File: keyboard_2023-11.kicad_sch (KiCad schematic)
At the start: 74 parts, among them J1 Conn_01x04, J11 Conn_01x07_Socket, J2 Conn_01x04_Socket, J3 Conn_01x07_Socket, J4 Conn_01x07_Pin, SW1 SW_Push, SW10 SW_Push, SW11 SW_Push, SW12 SW_Push, SW13 SW_Push, SW14 SW_Push, SW15 SW_Push, SW16 SW_Push, SW17 SW_Push, SW18 SW_Push, SW19 SW_Push, SW2 SW_Push, SW20 SW_Push, SW21 SW_Push, SW22 SW_Push, SW23 SW_Push, SW24 SW_Push, SW3 SW_Push, SW4 SW_Push, SW5 SW_Push, SW6 SW_Push, SW7 SW_Push, SW8 SW_Push, SW9 SW_Push, U1 MCP23017_SO, U2 MCP23017_SO

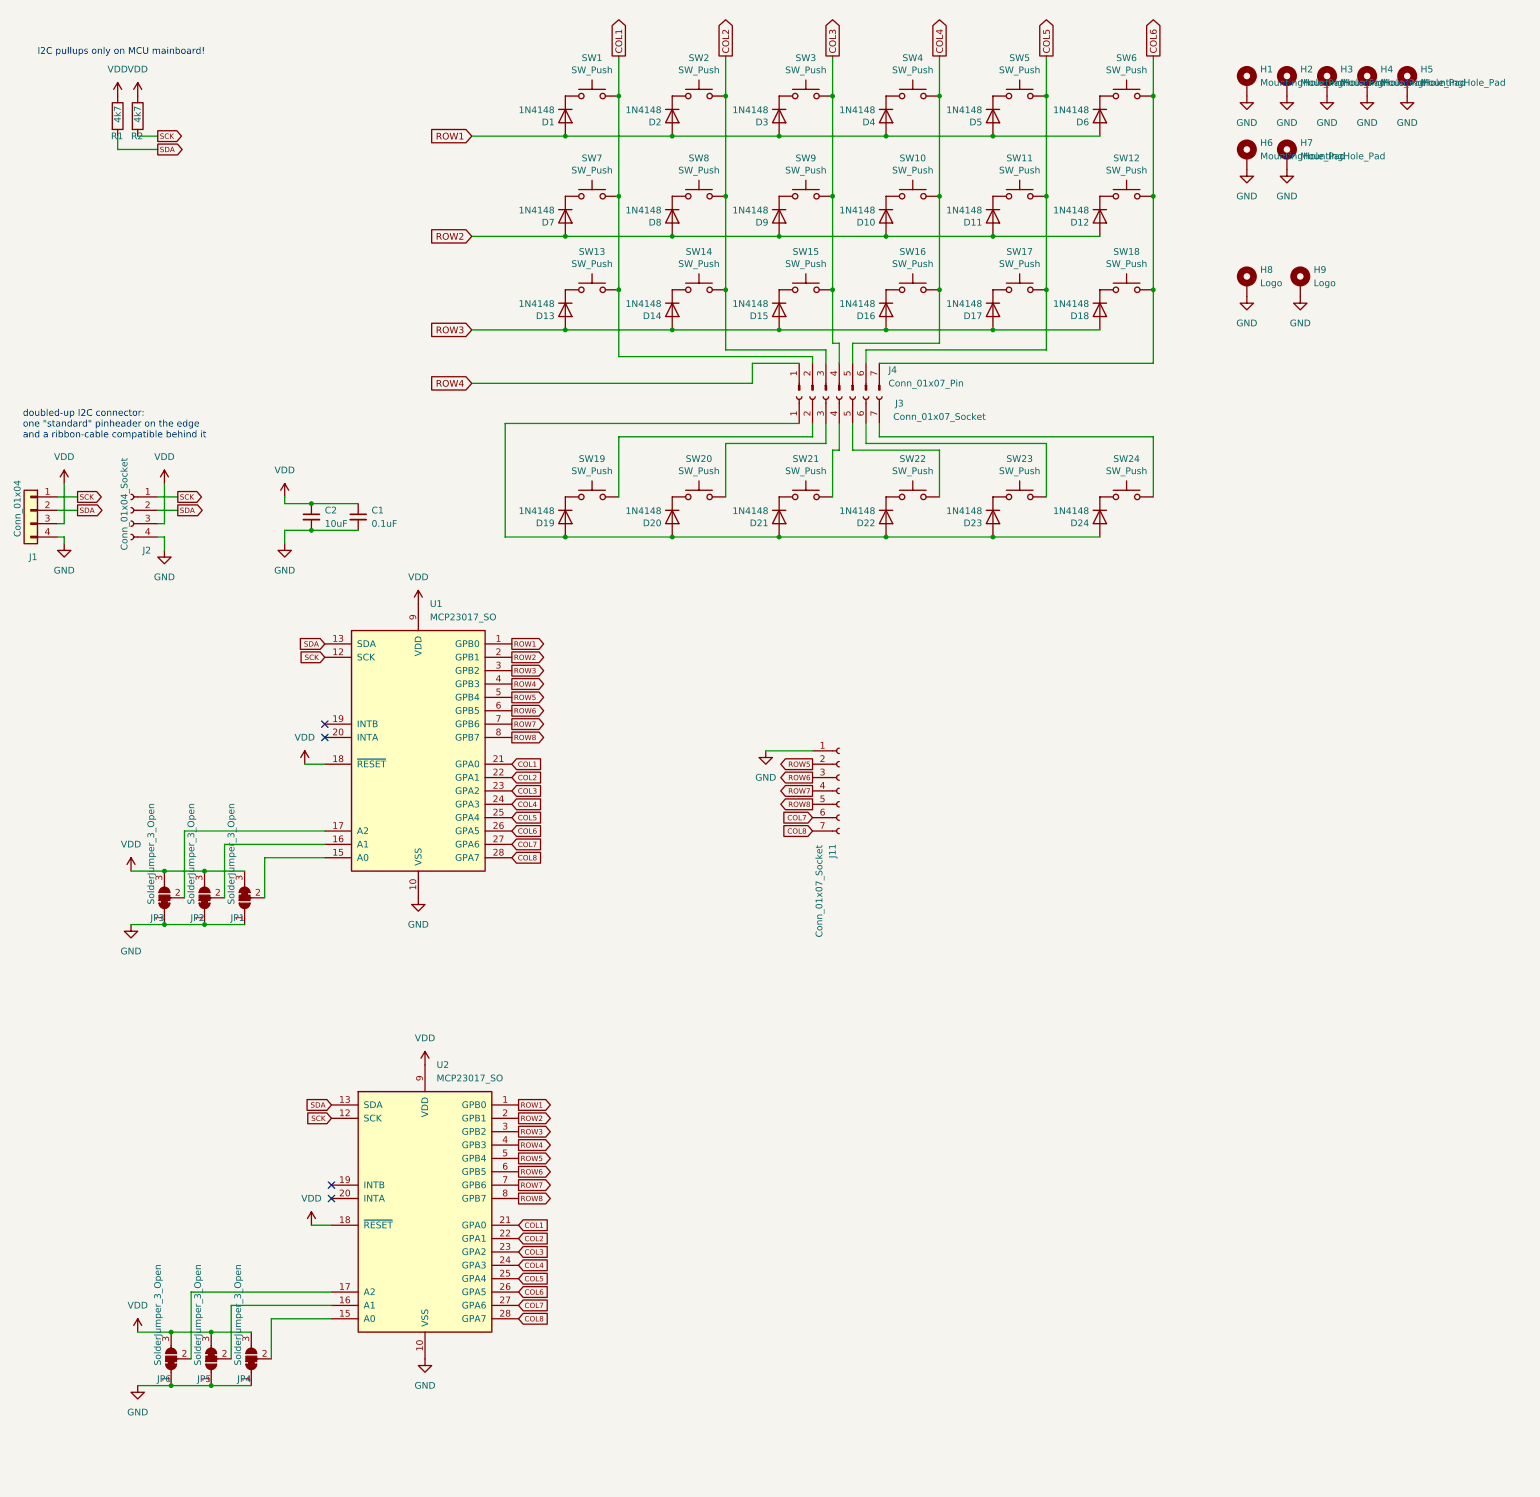
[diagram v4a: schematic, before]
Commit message: V2: gerber 2 JLCPCB
additional i2c ports
mounting "tab" for thumb cluster
nudged rows 3 (ringfinter) and 4 (middlefinger) a bit down
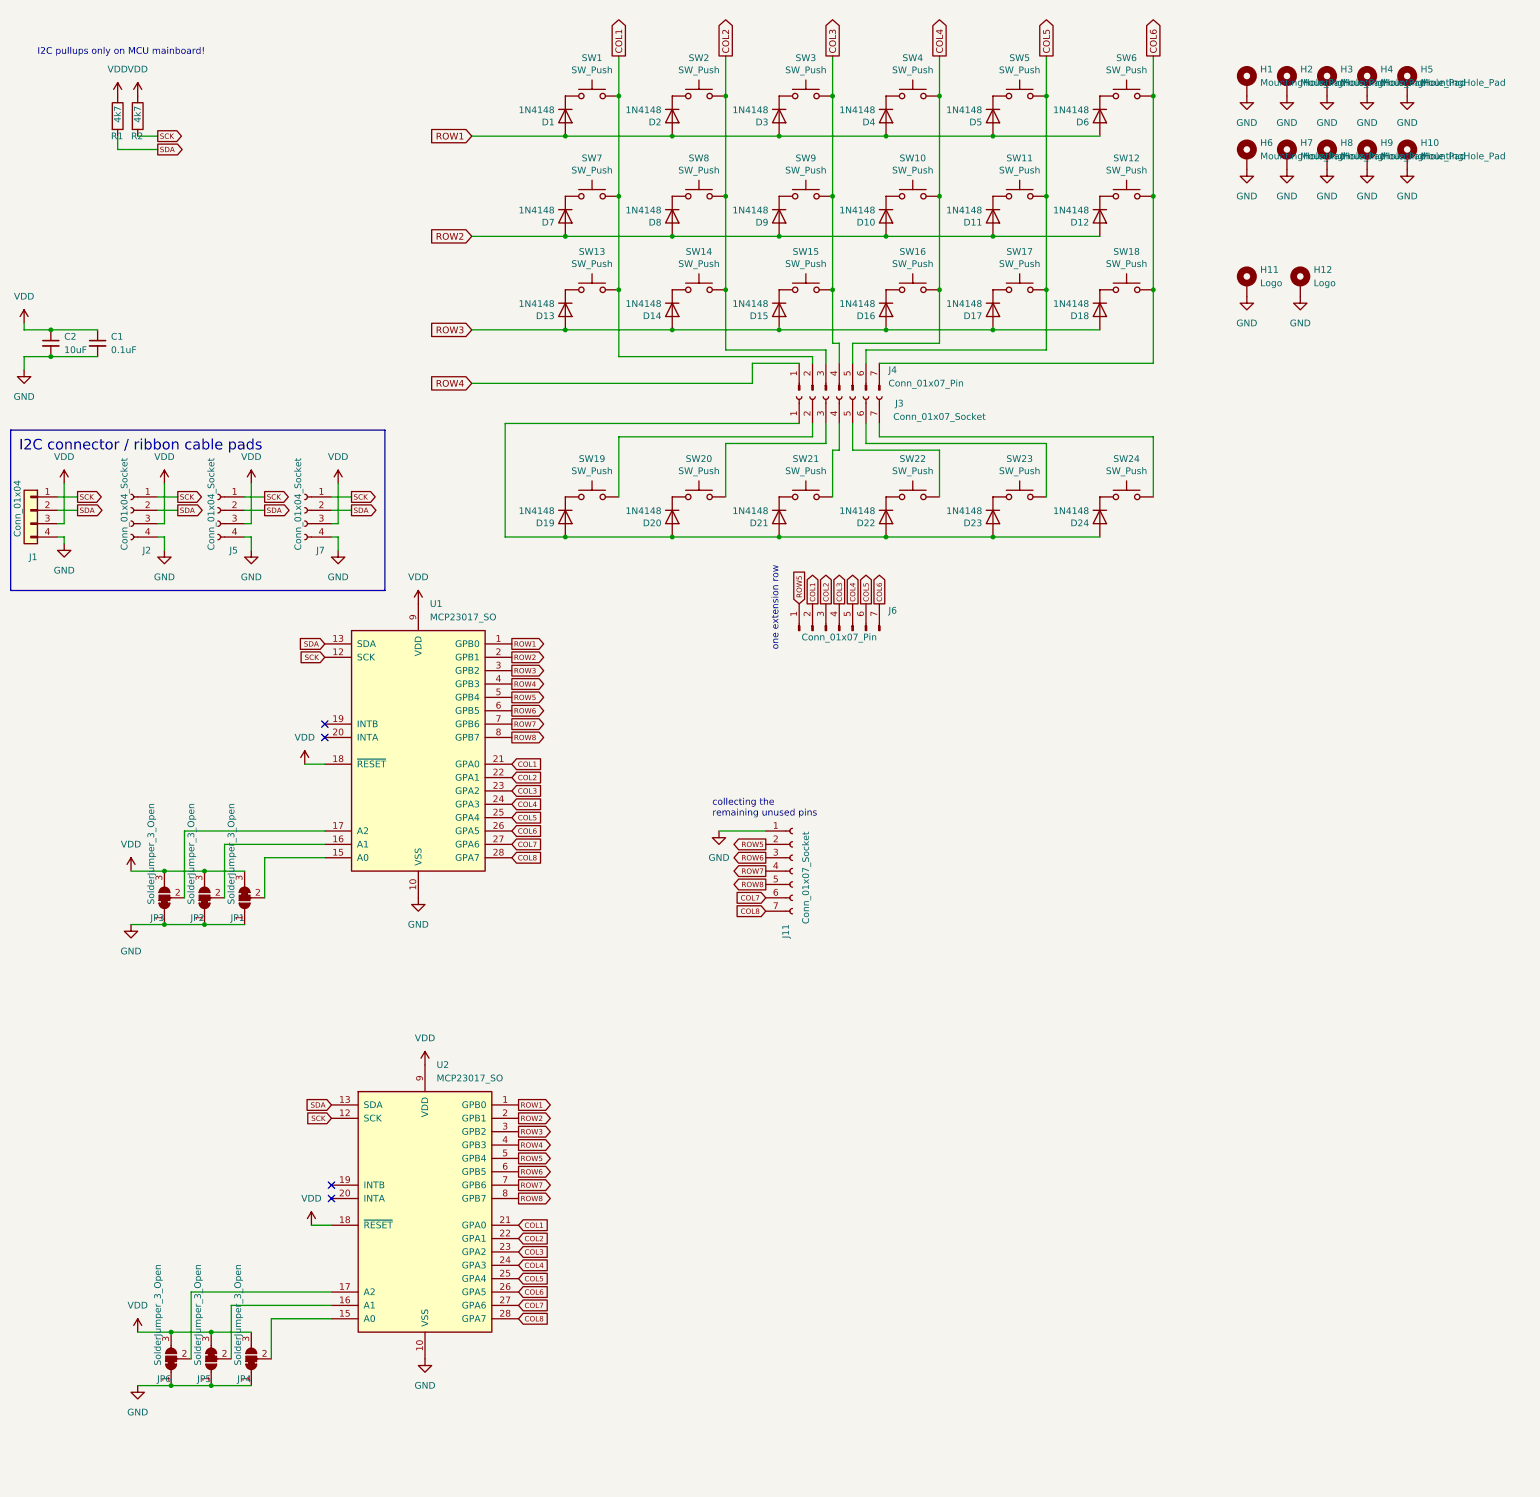
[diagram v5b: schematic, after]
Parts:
- added H10, H8, H9: MountingHole_Pad, project-local:MountingHole_3.2mm_M3_Pad_Via, symbol Mechanical:MountingHole_Pad
- added J5, J7: Conn_01x04_Socket, project-local:PinHeader_1x04_P1.27mm_Vertical, symbol Connector:Conn_01x04_Socket
- added J6: Conn_01x07_Pin, project-local:PinHeader_1x07_P1.27mm_Vertical, symbol Connector:Conn_01x07_Pin
- renumbered H8 to H11, H9 to H12
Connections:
- net COL1: now also J6.2 (Pin_2)
- net COL2: now also J6.3 (Pin_3)
- net COL3: now also J6.4 (Pin_4)
- net COL4: now also J6.5 (Pin_5)
- net COL5: now also J6.6 (Pin_6)
- net COL6: now also J6.7 (Pin_7)
- net GND: now also H10.1, H8.1, H9.1, J5.4 (Pin_4), J7.4 (Pin_4)
- net ROW5: now also J6.1 (Pin_1)
- net SCK: now also J5.1 (Pin_1), J7.1 (Pin_1)
- net SDA: now also J5.2 (Pin_2), J7.2 (Pin_2)
- net VDD: now also J5.3 (Pin_3), J7.3 (Pin_3)
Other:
- note added: "collecting the remaining unused pins"
- note added: "one extension row"
- moved on the sheet: C1, C2, J11

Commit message: c-numbering from 0 for columns&rows
to better align with the firmware, count from 0 instead of from 1
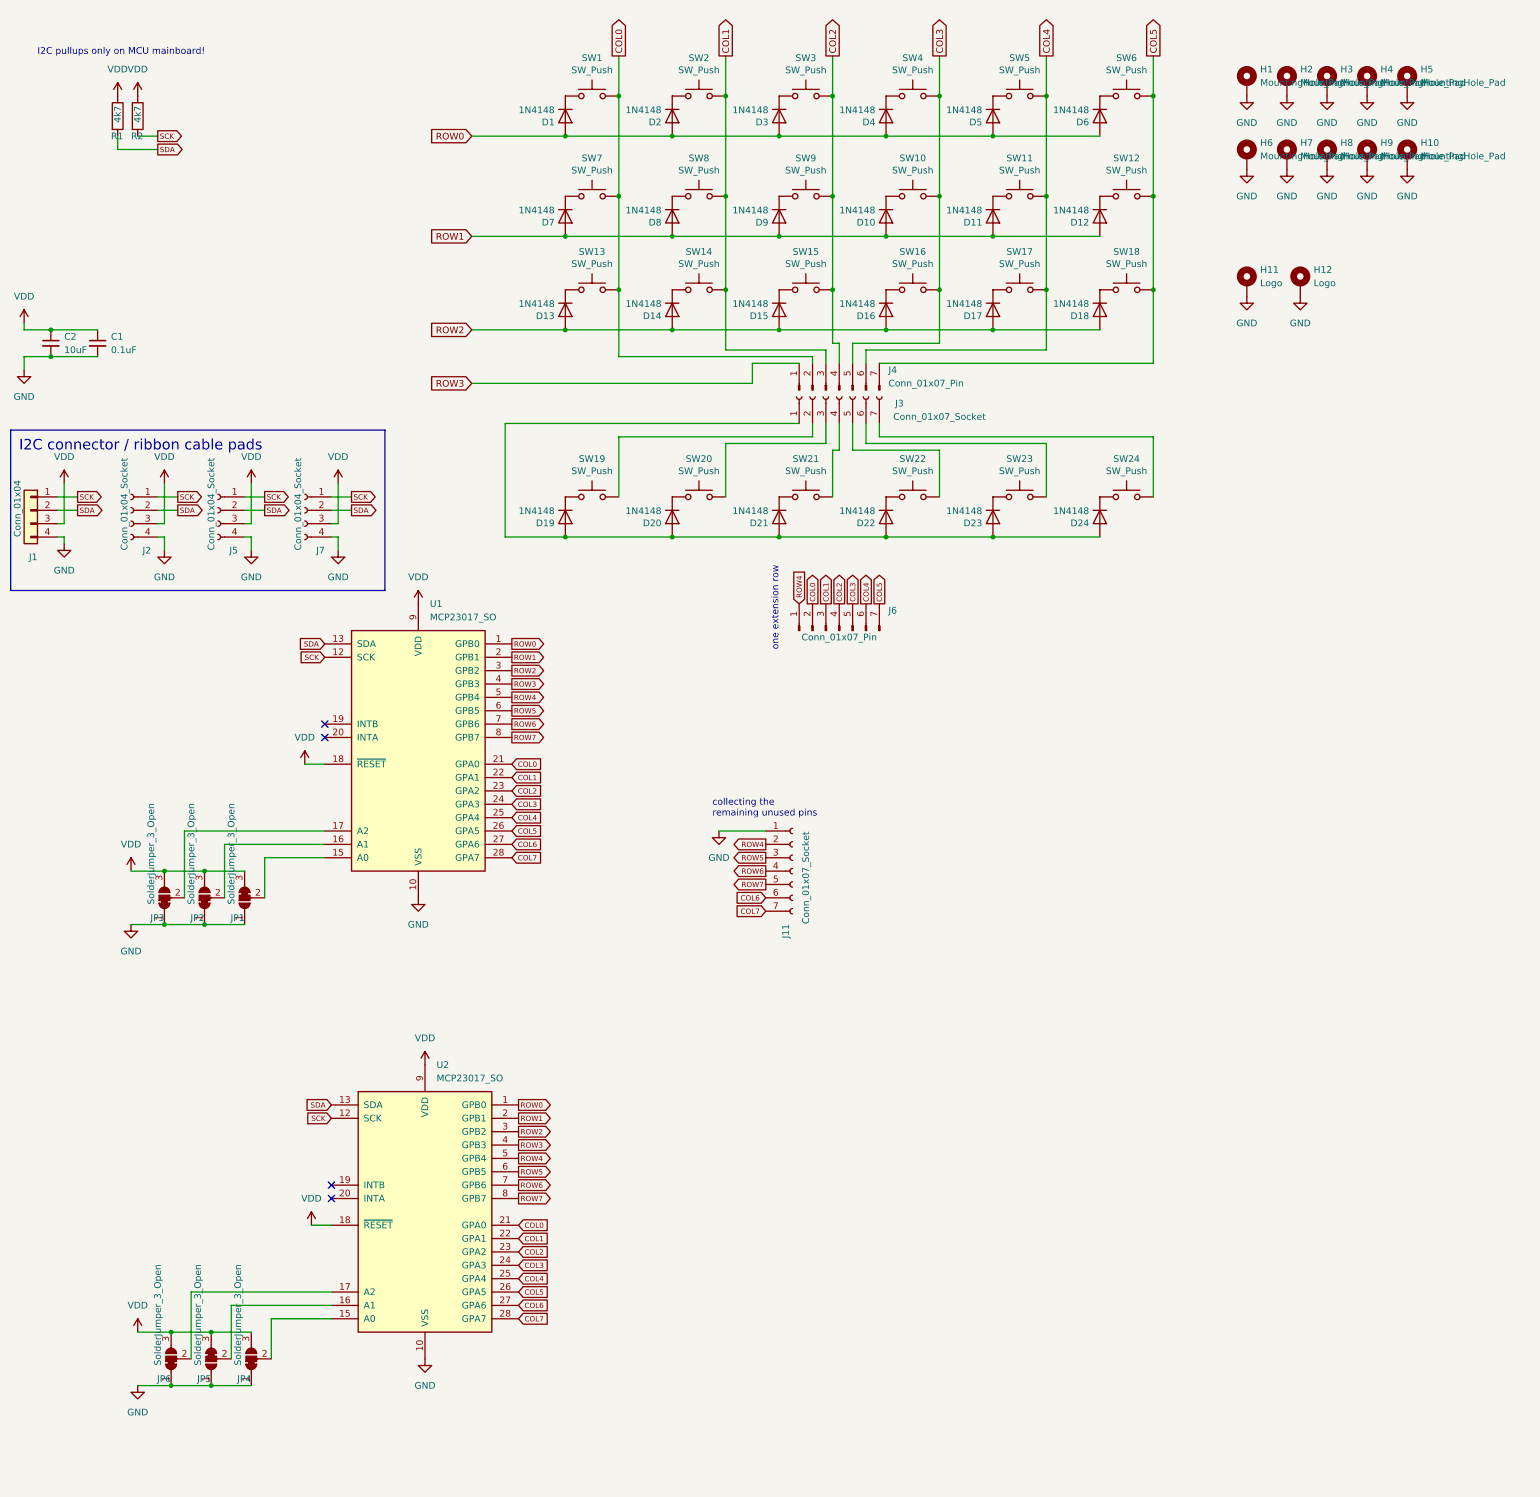
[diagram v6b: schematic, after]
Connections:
- net COL8 is gone; now on net COL7: J11.7 (Pin_7), U1.28 (GPA7), U2.28 (GPA7)
- net ROW8 is gone; now on net ROW7: J11.5 (Pin_5), U1.8 (GPB7), U2.8 (GPB7)
- net COL1: now also J4.3 (Pin_3), J6.3 (Pin_3), SW14.2, SW2.2, SW8.2, U1.22 (GPA1), U2.22 (GPA1); no longer J4.2 (Pin_2), J6.2 (Pin_2), SW1.2, SW13.2, SW7.2, U1.21 (GPA0), U2.21 (GPA0)
- net COL2: now also J4.4 (Pin_4), J6.4 (Pin_4), SW15.2, SW3.2, SW9.2, U1.23 (GPA2), U2.23 (GPA2); no longer J4.3 (Pin_3), J6.3 (Pin_3), SW14.2, SW2.2, SW8.2, U1.22 (GPA1), U2.22 (GPA1)
- net COL3: now also J4.5 (Pin_5), J6.5 (Pin_5), SW10.2, SW16.2, SW4.2, U1.24 (GPA3), U2.24 (GPA3); no longer J4.4 (Pin_4), J6.4 (Pin_4), SW15.2, SW3.2, SW9.2, U1.23 (GPA2), U2.23 (GPA2)
- net COL4: now also J4.6 (Pin_6), J6.6 (Pin_6), SW11.2, SW17.2, SW5.2, U1.25 (GPA4), U2.25 (GPA4); no longer J4.5 (Pin_5), J6.5 (Pin_5), SW10.2, SW16.2, SW4.2, U1.24 (GPA3), U2.24 (GPA3)
- net COL5: now also J4.7 (Pin_7), J6.7 (Pin_7), SW12.2, SW18.2, SW6.2, U1.26 (GPA5), U2.26 (GPA5); no longer J4.6 (Pin_6), J6.6 (Pin_6), SW11.2, SW17.2, SW5.2, U1.25 (GPA4), U2.25 (GPA4)
- net COL6: now also J11.6 (Pin_6), U1.27 (GPA6), U2.27 (GPA6); no longer J4.7 (Pin_7), J6.7 (Pin_7), SW12.2, SW18.2, SW6.2, U1.26 (GPA5), U2.26 (GPA5)
- net COL7: no longer J11.6 (Pin_6), U1.27 (GPA6), U2.27 (GPA6)
- net ROW1: now also D10.2 (A), D11.2 (A), D12.2 (A), D7.2 (A), D8.2 (A), D9.2 (A), U1.2 (GPB1), U2.2 (GPB1); no longer D1.2 (A), D2.2 (A), D3.2 (A), D4.2 (A), D5.2 (A), D6.2 (A), U1.1 (GPB0), U2.1 (GPB0)
- net ROW2: now also D13.2 (A), D14.2 (A), D15.2 (A), D16.2 (A), D17.2 (A), D18.2 (A), U1.3 (GPB2), U2.3 (GPB2); no longer D10.2 (A), D11.2 (A), D12.2 (A), D7.2 (A), D8.2 (A), D9.2 (A), U1.2 (GPB1), U2.2 (GPB1)
- net ROW3: now also J4.1 (Pin_1), U1.4 (GPB3), U2.4 (GPB3); no longer D13.2 (A), D14.2 (A), D15.2 (A), D16.2 (A), D17.2 (A), D18.2 (A), U1.3 (GPB2), U2.3 (GPB2)
- net ROW4: now also J11.2 (Pin_2), J6.1 (Pin_1), U1.5 (GPB4), U2.5 (GPB4); no longer J4.1 (Pin_1), U1.4 (GPB3), U2.4 (GPB3)
- net ROW5: now also J11.3 (Pin_3), U1.6 (GPB5), U2.6 (GPB5); no longer J11.2 (Pin_2), J6.1 (Pin_1), U1.5 (GPB4), U2.5 (GPB4)
- net ROW6: now also J11.4 (Pin_4), U1.7 (GPB6), U2.7 (GPB6); no longer J11.3 (Pin_3), U1.6 (GPB5), U2.6 (GPB5)
- net ROW7: no longer J11.4 (Pin_4), U1.7 (GPB6), U2.7 (GPB6)
- new net COL0: J4.2 (Pin_2), J6.2 (Pin_2), SW1.2, SW13.2, SW7.2, U1.21 (GPA0), U2.21 (GPA0)
- new net ROW0: D1.2 (A), D2.2 (A), D3.2 (A), D4.2 (A), D5.2 (A), D6.2 (A), U1.1 (GPB0), U2.1 (GPB0)

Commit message: cleanup schematic for release
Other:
- note added: "left/right side IO-expander only on is populated with its address preconfigured by jumpers on the opposite side of the pcb"
- moved on the sheet: C1, C2, D1, D10, D11, D12, D13, D14, D15, D16, D17, D18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
